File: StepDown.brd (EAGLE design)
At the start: 100 x 80 mm, 18 parts, among them IC1 TL494CN, T1 TIP32A

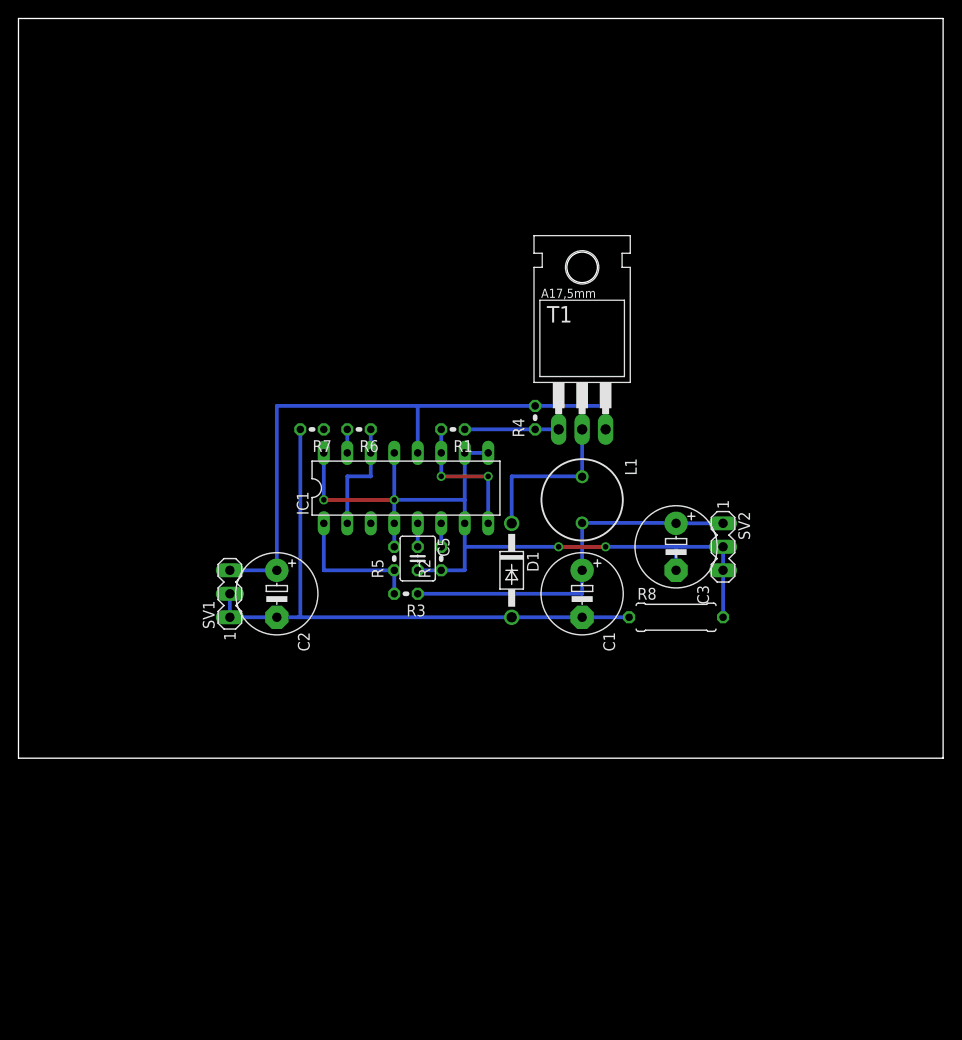
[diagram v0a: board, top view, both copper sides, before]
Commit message: Add current sense (not tested)
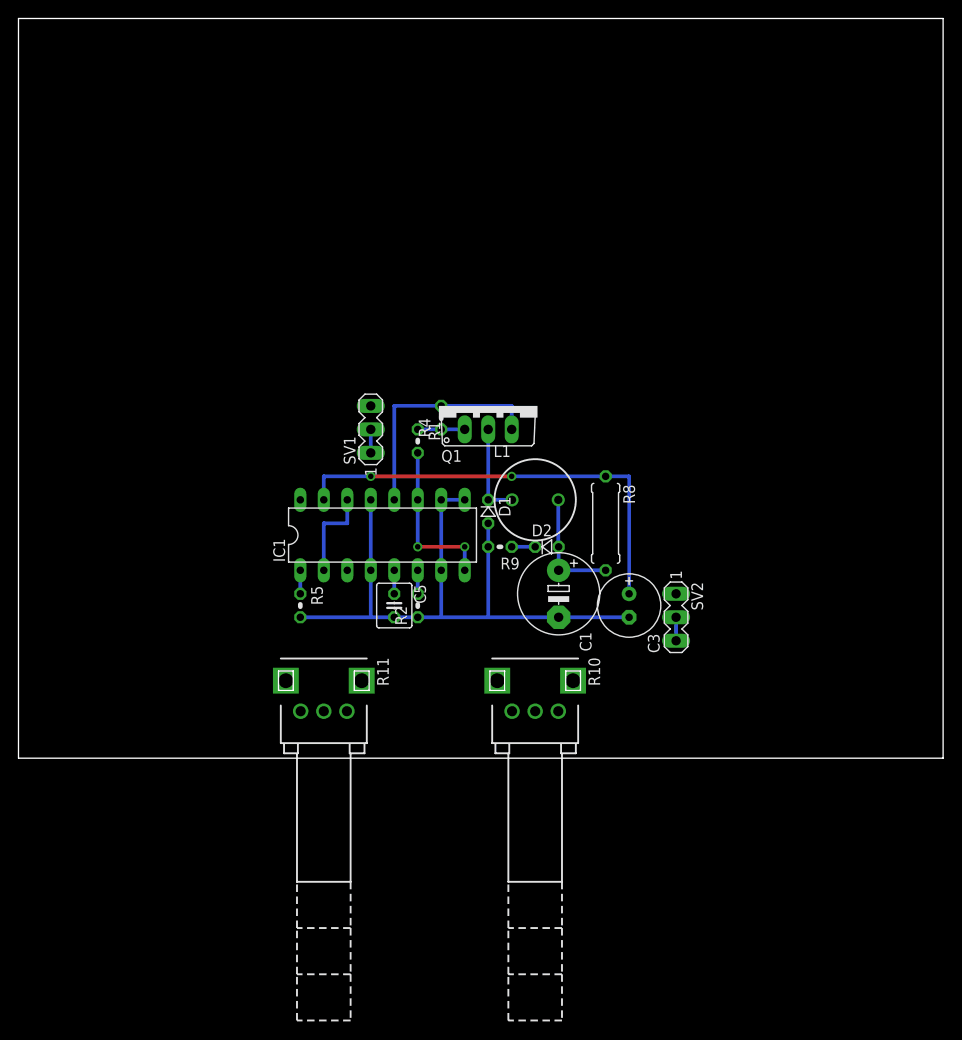
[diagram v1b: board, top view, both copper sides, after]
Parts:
- removed C2: 50µ, rcl:E5-8,5
- removed R3: 1k, rcl:0204V
- removed R6: 5k1, rcl:0204V
- removed R7: 150, rcl:0204V
- removed T1: TIP32A, transistor:TO220
- added D2: (no value), diode:D-2.5
- added Q1: TIP42C, transistor-power:TO220AV
- added R10, R11: 50k, pot:EVUE
- added R9: 10k, rcl:0204V
- C3: device rcl:E5-8,5 -> rcl:E2,5-7
- D1: value 1N4004 -> (none); device diode:DO41-10 -> diode:D-2.5
- R5: value 470 -> 10k
- moved SV1 23.4 mm to (38.1, 35.6)
- moved R8 12.7 mm to (63.5, 25.4), turned to 270 degrees
- moved R5 11.4 mm to (30.5, 16.5), turned to 270 degrees
- moved R4 10.2 mm to (45.7, 36.8)
- moved SV2 9.16 mm to (71.1, 15.2)
- moved C3 8.13 mm to (66.0, 16.5)
- moved D1 6.84 mm to (50.8, 26.7)
- moved IC1 5.68 mm to (39.4, 24.1)
- moved C5 5.68 mm to (40.6, 16.5)
- moved R2 5.68 mm to (43.2, 16.5)
- moved L1 5.08 mm to (55.9, 27.9), turned to 0 degrees
- moved R1 4.02 mm to (43.2, 34.3), turned to 270 degrees
- moved C1 2.54 mm to (58.4, 17.8)
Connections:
- removed net N$14: C3.-, C5.2, IC1.10, IC1.13, IC1.16, IC1.4, IC1.7, IC1.9, R2.1, R5.2, R8.2, SV2.2, SV2.3
- new net N$12: C1.-, C3.-, C5.2, D1.A, IC1.10, IC1.13, IC1.4, IC1.7, IC1.9, R2.1, R5.2, R9.2, SV1.1, SV1.2, SV2.2, SV2.3
- new net N$4: C1.+, D2.A, L1.2, R10.1, R8.2
- net N$1: now also Q1.E; no longer C2.+, T1.3
- net N$10: now also IC1.15, R11.1, R8.1; no longer C1.+, L1.2, R3.1
- net N$11: now also R11.2, R11.3; no longer R3.2
- net N$13: now also D2.C, R10.3, R9.1; no longer IC1.15, R6.2, R7.1
- net N$3: no longer R6.1
- net N$5: now also IC1.16, R10.2; no longer C1.-, C2.-, D1.A, R7.2, R8.1, SV1.1, SV1.2
- net N$7: now also Q1.B; no longer T1.1
- net N$9: now also Q1.C; no longer T1.2
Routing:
- net N$14: track 88.9 -> 0.00 mm, vias 4 -> 0
- net N$12: track 0.00 -> 78.7 mm
- net N$5: track 66.0 -> 0.00 mm
- net N$1: track 66.0 -> 25.4 mm
- net N$4: track 0.00 -> 12.8 mm
- net N$11: track 15.2 -> 2.54 mm
- net N$9: track 17.9 -> 10.2 mm
- net N$10: track 40.7 -> 48.3 mm, vias 0 -> 2
- net N$7: track 10.2 -> 5.08 mm
- net N$3: track 12.7 -> 10.2 mm
- net N$8: track 15.2 -> 17.8 mm

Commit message: Use MOSFET for more than 25A (tested and working)
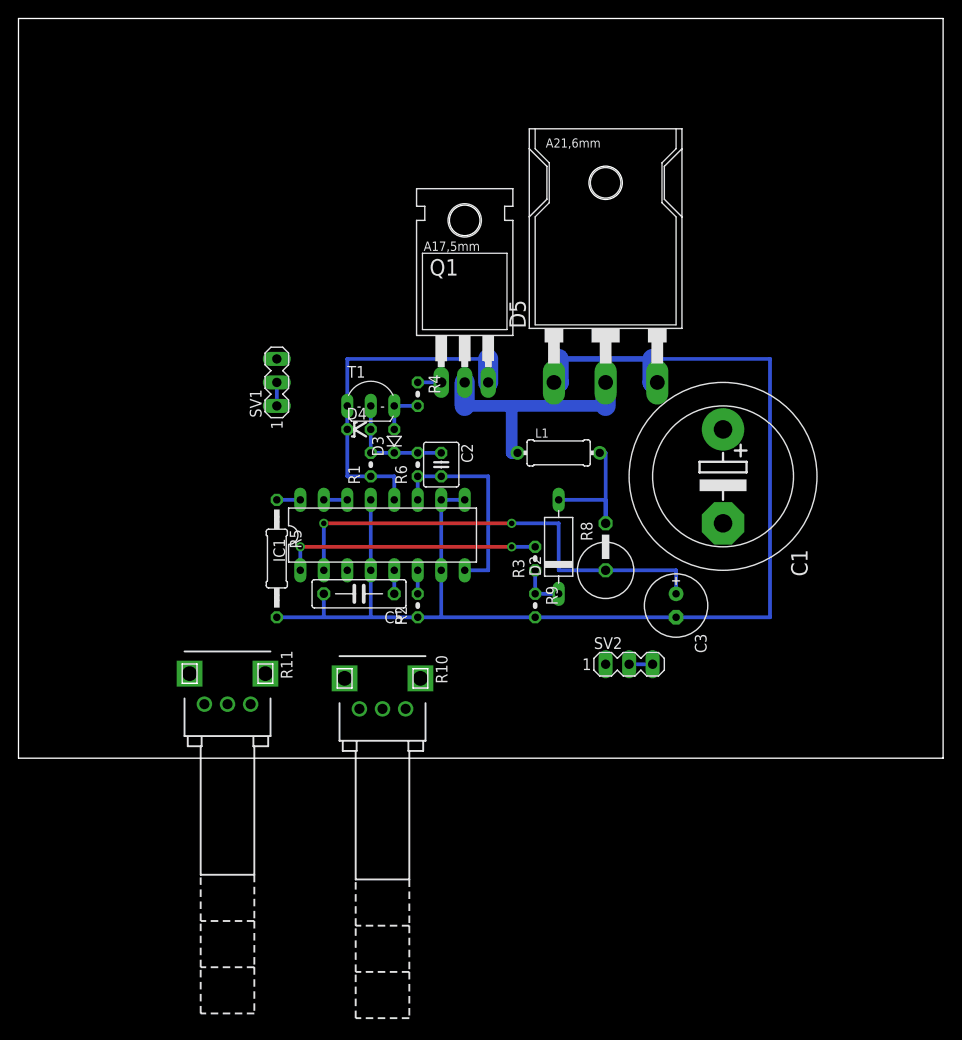
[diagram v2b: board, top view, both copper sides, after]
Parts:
- removed D1: (no value), diode:D-2.5
- added C2: 1n, rcl:C025-040X050
- added D3: 1N4148, diode:D-2.5
- added D4: 10V, diode:ZDIO-2.5
- added D5: MBR2545, diode:TO3P
- added R3: 10k, rcl:0204V
- added R6: 1k, rcl:0204V
- added T1: BC547, transistor:TO92-CBE
- C1: value 500µ -> 4700µ; device rcl:E5-8,5 -> rcl:EB20D
- C5: value 1n -> 10n; device rcl:C025-040X050 -> rcl:C075-032X103
- D2: device diode:D-2.5 -> diode:D-10
- L1: value 1m -> 10µ; device rcl:6000-XXXX-RC -> rcl:TFI0307
- Q1: value TIP42C -> IRF4905; device transistor-power:TO220AV -> transistor-power:TO220BH
- R1: value 150 -> 1k
- R10, R11: value 50k -> 10k
- R2: value 47k -> 10k
- R4: value 47 -> 47R
- R5: value 10k -> 2k; device rcl:0204V -> rcl:0207/12
- R8: value 0.1Ohm -> 0.01R; device rcl:0309/10 -> rcl:0617V
- moved C1 21.8 mm to (76.2, 30.5)
- moved R10 16.5 mm to (39.4, 5.33)
- moved SV1 11.4 mm to (27.9, 40.6)
- moved R11 10.4 mm to (22.6, 5.84)
- moved Q1 9.25 mm to (48.3, 47.0)
- moved R9 7.41 mm to (55.9, 16.5), turned to 270 degrees
- moved SV2 7.18 mm to (66.0, 10.2), turned to 0 degrees
- moved L1 5.68 mm to (58.4, 33.0)
- moved R1 5.68 mm to (38.1, 31.8), turned to 90 degrees
- moved R5 5.68 mm to (27.9, 21.6)
- moved C3 5.08 mm to (71.1, 16.5)
- moved C5 4.02 mm to (36.8, 17.8), turned to 180 degrees
- moved R4 3.59 mm to (43.2, 39.4), turned to 270 degrees
- moved R8 2.54 mm to (63.5, 22.9), turned to 90 degrees
- moved D2 1.27 mm to (58.4, 22.9), turned to 90 degrees
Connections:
- removed net N$12: C1.-, C3.-, C5.2, D1.A, IC1.10, IC1.13, IC1.4, IC1.7, IC1.9, R2.1, R5.2, R9.2, SV1.1, SV1.2, SV2.2, SV2.3
- new net +24V: D4.C, IC1.12, Q1.S, R1.1, SV1.3, T1.C
- new net GND: C1.-, C3.-, C5.2, D5.1, D5.3, IC1.10, IC1.13, IC1.4, IC1.7, IC1.9, R2.1, R5.2, R9.2, SV1.1, SV1.2, SV2.2, SV2.3
- new net N$14: Q1.G, R4.1
- net N$1: now also C2.2, IC1.11, IC1.8, R6.1; no longer IC1.12, Q1.E, R4.2, SV1.3
- net N$10: now also IC1.2; no longer IC1.15
- net N$11: now also IC1.16; no longer IC1.1
- net N$13: now also R3.1; no longer R10.3
- net N$3: now also IC1.15; no longer IC1.2
- net N$5: now also IC1.1, R10.3, R3.2; no longer IC1.16
- net N$7: now also D3.A, R4.2, T1.E; no longer Q1.B, R1.1, R4.1
- net N$8: now also C2.1, D3.C, D4.A, R6.2, T1.B; no longer IC1.11, IC1.8
- net N$9: now also D5.2, Q1.D; no longer D1.C, Q1.C
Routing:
- net GND: track 0.00 -> 145.8 mm
- net N$12: track 78.7 -> 0.00 mm
- net +24V: track 0.00 -> 38.1 mm
- net N$5: track 0.00 -> 27.9 mm, vias 0 -> 2
- net N$9: track 10.2 -> 26.0 mm
- net N$3: track 10.2 -> 2.54 mm
- net N$8: track 17.8 -> 12.7 mm, vias 2 -> 0
- net N$4: track 12.8 -> 15.9 mm
- net N$1: track 25.4 -> 22.9 mm
- net N$14: track 0.00 -> 2.54 mm
- net N$13: track 2.54 -> 5.08 mm
- net N$10: track 48.3 -> 50.8 mm
